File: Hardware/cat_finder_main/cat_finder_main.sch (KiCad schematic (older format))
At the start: 32 parts, among them J1 BATT, J10 Analog, J2 BME280, J3 CSS811, J4 DRIVERS, J5 GY-87, J6 Prog, J7 FTDI, J8 Digital, J9 i2c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

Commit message: clone other repo
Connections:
- net INTCSS is gone; now on net +3V3: J3.6 (Pin_6)
- net RESET is gone; now on net +3V3: J3.7 (Pin_7)
- net WAKE is gone; now on net GND: J3.5 (Pin_5)
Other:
- moved on the sheet: JP10, JP5, JP6, JP7, JP8, JP9
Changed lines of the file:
@@
 	1760 6310 2010 6310
-$Comp
-L power:GND #PWR09
-U 1 1 5D24666B
-P 3280 6200
-F 0 "#PWR09" H 3280 5950 50  0001 C CNN
-F 1 "GND" H 3285 6027 50  0000 C CNN
-F 2 "" H 3280 6200 50  0001 C CNN
-F 3 "" H 3280 6200 50  0001 C CNN
-	1    3280 6200
-	1    0    0    -1
-$EndComp
 $Comp
 L power:+3.3V #PWR08
@@
 Wire Wire Line
 	3280 6060 3570 6060
-Wire Wire Line
-	3280 6200 3280 6160
-Wire Wire Line
-	3280 6160 3570 6160
 $Comp
 L rover_main-rescue:MCP732831CHARGER-electroniccats U2
@@
 	0    -1   -1   0
 $EndComp
-Text Label 10400 4800 0    50   ~ 0
+Text Label 10760 4600 0    50   ~ 0
 SCL
-Text Label 10400 4400 0    50   ~ 0
+Text Label 10760 4300 0    50   ~ 0
 SDA
-Text Label 9800 4400 2    50   ~ 0
+Text Label 10160 4300 2    50   ~ 0
 SDAB
 Text Label 8450 6050 3    50   ~ 0
 SDAB
-Text Label 9800 4800 2    50   ~ 0
+Text Label 10160 4600 2    50   ~ 0
 SCLB
 Text Label 8550 6050 3    50   ~ 0
 SCLB
-Text Label 9800 6000 2    50   ~ 0
+Text Label 10150 5500 2    50   ~ 0
 A3
-Text Label 10400 5600 0    50   ~ 0
+Text Label 10750 5210 0    50   ~ 0
 GPIO12
-Text Label 10400 5200 0    50   ~ 0
+Text Label 10750 4900 0    50   ~ 0
 GPIO13
-Text Label 10400 6000 0    50   ~ 0
+Text Label 10750 5500 0    50   ~ 0
 GPIO15
-Text Label 10380 6400 0    50   ~ 0
+Text Label 10700 5800 0    50   ~ 0
 GPIO14
 $Comp
@@
 Text Label 5290 6000 2    50   ~ 0
 VCC-IN
-Text Label 9800 5600 2    50   ~ 0
+Text Label 10150 5210 2    50   ~ 0
 11
-Text Label 9800 5200 2    50   ~ 0
+Text Label 10150 4900 2    50   ~ 0
 A1
-Text Label 9820 6400 2    50   ~ 0
+Text Label 10140 5800 2    50   ~ 0
 9
 $Comp
@@
 L Device:Jumper_NO_Small JP5
 U 1 1 5D4C5CB0
-P 10080 4400
-F 0 "JP5" H 10080 4585 50  0000 C CNN
-F 1 "SDA" H 10080 4494 50  0000 C CNN
-F 2 "Jumper:SolderJumper-2_P1.3mm_Open_RoundedPad1.0x1.5mm" H 10080 4400 50  0001 C CNN
-F 3 "~" H 10080 4400 50  0001 C CNN
-	1    10080 4400
+P 10440 4300
+F 0 "JP5" H 10440 4485 50  0000 C CNN
+F 1 "SDA" H 10440 4394 50  0000 C CNN
+F 2 "Jumper:SolderJumper-2_P1.3mm_Open_RoundedPad1.0x1.5mm" H 10440 4300 50  0001 C CNN
+F 3 "~" H 10440 4300 50  0001 C CNN
+	1    10440 4300
 	1    0    0    -1
 $EndComp
@@
 L Device:Jumper_NO_Small JP6
 U 1 1 5D4C667E
-P 10100 4800
-F 0 "JP6" H 10100 4985 50  0000 C CNN
-F 1 "SCL" H 10100 4894 50  0000 C CNN
-F 2 "Jumper:SolderJumper-2_P1.3mm_Open_RoundedPad1.0x1.5mm" H 10100 4800 50  0001 C CNN
-F 3 "~" H 10100 4800 50  0001 C CNN
-	1    10100 4800
-	1    0    0    -1
-$EndComp
-Wire Wire Line
-	10180 4400 10400 4400
-Wire Wire Line
-	9980 4400 9800 4400
-Wire Wire Line
-	10400 4800 10200 4800
-Wire Wire Line
-	9800 4800 10000 4800
+P 10460 4600
+F 0 "JP6" H 10460 4785 50  0000 C CNN
+F 1 "SCL" H 10460 4694 50  0000 C CNN
+F 2 "Jumper:SolderJumper-2_P1.3mm_Open_RoundedPad1.0x1.5mm" H 10460 4600 50  0001 C CNN
+F 3 "~" H 10460 4600 50  0001 C CNN
+	1    10460 4600
+	1    0    0    -1
+$EndComp
+Wire Wire Line
+	10540 4300 10760 4300
+Wire Wire Line
+	10340 4300 10160 4300
+Wire Wire Line
+	10760 4600 10560 4600
+Wire Wire Line
+	10160 4600 10360 4600
 $Comp
 L Device:Jumper_NO_Small JP7
 U 1 1 5D4CD611
-P 10120 5200
-F 0 "JP7" H 10120 5385 50  0000 C CNN
-F 1 "Engine 1 A" H 10120 5294 50  0000 C CNN
-F 2 "Jumper:SolderJumper-2_P1.3mm_Open_RoundedPad1.0x1.5mm" H 10120 5200 50  0001 C CNN
-F 3 "~" H 10120 5200 50  0001 C CNN
-	1    10120 5200
-	1    0    0    -1
-$EndComp
-Wire Wire Line
-	10220 5200 10400 5200
-Wire Wire Line
-	10020 5200 9800 5200
+P 10470 4900
+F 0 "JP7" H 10470 5085 50  0000 C CNN
+F 1 "Engine 1 A" H 10470 4994 50  0000 C CNN
+F 2 "Jumper:SolderJumper-2_P1.3mm_Open_RoundedPad1.0x1.5mm" H 10470 4900 50  0001 C CNN
+F 3 "~" H 10470 4900 50  0001 C CNN
+	1    10470 4900
+	1    0    0    -1
+$EndComp
+Wire Wire Line
+	10570 4900 10750 4900
+Wire Wire Line
+	10370 4900 10150 4900
 $Comp
 L Device:Jumper_NO_Small JP8
 U 1 1 5D4D2033
-P 10130 5600
-F 0 "JP8" H 10130 5785 50  0000 C CNN
-F 1 "Engine 1B" H 10130 5694 50  0000 C CNN
-F 2 "Jumper:SolderJumper-2_P1.3mm_Open_RoundedPad1.0x1.5mm" H 10130 5600 50  0001 C CNN
-F 3 "~" H 10130 5600 50  0001 C CNN
-	1    10130 5600
-	1    0    0    -1
-$EndComp
-Wire Wire Line
-	10230 5600 10400 5600
-Wire Wire Line
-	10030 5600 9800 5600
+P 10480 5210
+F 0 "JP8" H 10480 5395 50  0000 C CNN
+F 1 "Engine 1B" H 10480 5304 50  0000 C CNN
+F 2 "Jumper:SolderJumper-2_P1.3mm_Open_RoundedPad1.0x1.5mm" H 10480 5210 50  0001 C CNN
+F 3 "~" H 10480 5210 50  0001 C CNN
+	1    10480 5210
+	1    0    0    -1
+$EndComp
+Wire Wire Line
+	10580 5210 10750 5210
+Wire Wire Line
+	10380 5210 10150 5210
 $Comp
 L Device:Jumper_NO_Small JP9
 U 1 1 5D4D5761
-P 10100 6000
-F 0 "JP9" H 10100 6185 50  0000 C CNN
-F 1 "Engine 2A" H 10100 6094 50  0000 C CNN
-F 2 "Jumper:SolderJumper-2_P1.3mm_Open_RoundedPad1.0x1.5mm" H 10100 6000 50  0001 C CNN
-F 3 "~" H 10100 6000 50  0001 C CNN
-	1    10100 6000
-	1    0    0    -1
-$EndComp
-Wire Wire Line
-	10200 6000 10400 6000
-Wire Wire Line
-	9800 6000 10000 6000
+P 10450 5500
+F 0 "JP9" H 10450 5685 50  0000 C CNN
+F 1 "Engine 2A" H 10450 5594 50  0000 C CNN
+F 2 "Jumper:SolderJumper-2_P1.3mm_Open_RoundedPad1.0x1.5mm" H 10450 5500 50  0001 C CNN
+F 3 "~" H 10450 5500 50  0001 C CNN
+	1    10450 5500
+	1    0    0    -1
+$EndComp
+Wire Wire Line
+	10550 5500 10750 5500
+Wire Wire Line
+	10150 5500 10350 5500
 $Comp
 L Device:Jumper_NO_Small JP10
 U 1 1 5D4DA54D
-P 10100 6400
-F 0 "JP10" H 10100 6585 50  0000 C CNN
-F 1 "Engine 2B" H 10100 6494 50  0000 C CNN
-F 2 "Jumper:SolderJumper-2_P1.3mm_Open_RoundedPad1.0x1.5mm" H 10100 6400 50  0001 C CNN
-F 3 "~" H 10100 6400 50  0001 C CNN
-	1    10100 6400
-	1    0    0    -1
-$EndComp
-Wire Wire Line
-	10200 6400 10380 6400
-Wire Wire Line
-	10000 6400 9820 6400
+P 10420 5800
+F 0 "JP10" H 10420 5985 50  0000 C CNN
+F 1 "Engine 2B" H 10420 5894 50  0000 C CNN
+F 2 "Jumper:SolderJumper-2_P1.3mm_Open_RoundedPad1.0x1.5mm" H 10420 5800 50  0001 C CNN
+F 3 "~" H 10420 5800 50  0001 C CNN
+	1    10420 5800
+	1    0    0    -1
+$EndComp
+Wire Wire Line
+	10520 5800 10700 5800
+Wire Wire Line
+	10320 5800 10140 5800
+$Comp
+L power:+3.3V #PWR?
+U 1 1 5D54B969
+P 3000 6400
+F 0 "#PWR?" H 3000 6250 50  0001 C CNN
+F 1 "+3.3V" H 2840 6420 50  0000 C CNN
+F 2 "" H 3000 6400 50  0001 C CNN
+F 3 "" H 3000 6400 50  0001 C CNN
+	1    3000 6400
+	1    0    0    -1
+$EndComp
+$Comp
+L power:GND #PWR?
+U 1 1 5D544C06
+P 3200 6470
+F 0 "#PWR?" H 3200 6220 50  0001 C CNN
+F 1 "GND" H 3100 6470 50  0000 C CNN
+F 2 "" H 3200 6470 50  0001 C CNN
+F 3 "" H 3200 6470 50  0001 C CNN
+	1    3200 6470
+	1    0    0    -1
+$EndComp
+Wire Wire Line
+	3570 6460 3200 6460
+Wire Wire Line
+	3200 6460 3200 6470
+Wire Wire Line
+	3570 6160 3200 6160
+Wire Wire Line
+	3200 6160 3200 6460
+Connection ~ 3200 6460
+Wire Wire Line
+	3570 6560 3300 6560
+Wire Wire Line
+	3300 6560 3300 6660
+Wire Wire Line
+	3300 6660 3570 6660
+Wire Wire Line
+	3300 6660 3000 6660
+Connection ~ 3300 6660
+Wire Wire Line
+	3000 6660 3000 6400
 $EndSCHEMATC

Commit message: fix charger
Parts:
- removed U2: MCP732831CHARGER, Batteries:charger_EC_3.3V_battery, symbol rover_main-rescue:MCP732831CHARGER-electroniccats
- added U2: MCP732831CHARGER, Batteries:charger_EC_3.3V_battery, symbol electroniccats:MCP732831CHARGER
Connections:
- net BATT: now also U2.3 (OUT)
- net GND: now also U2.2 (GND), U2.4 (GND)
- net VCC: now also U2.1 (VCC)
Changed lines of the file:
@@
 EESchema Schematic File Version 4
-LIBS:rover_main-cache
 EELAYER 29 0
 EELAYER END
@@
 	3280 6060 3570 6060
 $Comp
-L rover_main-rescue:MCP732831CHARGER-electroniccats U2
-U 1 1 5D24ED12
-P 4180 3790
-F 0 "U2" H 4180 4205 50  0000 C CNN
-F 1 "MCP732831CHARGER" H 4180 4114 50  0000 C CNN
-F 2 "Batteries:charger_EC_3.3V_battery" H 4180 3790 50  0001 C CNN
-F 3 "" H 4180 3790 50  0001 C CNN
-F 4 "EC" H 4180 3790 50  0001 C CNN "manf#"
-	1    4180 3790
-	1    0    0    -1
-$EndComp
-$Comp
 L power:VCC #PWR05
 U 1 1 5D24F7E2
@@
 Wire Wire Line
 	3000 6660 3000 6400
+$Comp
+L electroniccats:MCP732831CHARGER U2
+U 1 1 5D6C735F
+P 4180 3790
+F 0 "U2" H 4180 4205 50  0000 C CNN
+F 1 "MCP732831CHARGER" H 4180 4114 50  0000 C CNN
+F 2 "Batteries:charger_EC_3.3V_battery" H 4180 3790 50  0001 C CNN
+F 3 "" H 4180 3790 50  0001 C CNN
+F 4 "EC" H 4180 3790 50  0001 C CNN "manf#"
+	1    4180 3790
+	1    0    0    -1
+$EndComp
 $EndSCHEMATC

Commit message: change drill esp32
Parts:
- removed U3: ESP32-CAM, Rf:ESP32-CAM, symbol rover_main-rescue:ESP32-CAM-electroniccats
- added U3: ESP32-CAM, Rf:ESP32-CAM, symbol electroniccats:ESP32-CAM
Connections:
- net +3V3: now also U3.8 (3V3)
- net 3.3V-5V: now also U3.4 (VCC)
- net 5V: now also U3.9 (5V)
- net GND: now also U3.1 (GND), U3.10 (GND), U3.5 (GND)
- net GPIO0: now also U3.6 (IO0)
- net GPIO12E: now also U3.11 (IO12)
- net GPIO13E: now also U3.12 (IO13)
- net GPIO14E: now also U3.14 (IO14)
- net GPIO15E: now also U3.13 (IO15)
- net GPIO2: now also U3.15 (IO2)
- net GPIO4: now also U3.16 (IO4)
- net RX: now also U3.3 (UnR)
- net SCLE: now also U3.7 (IO16)
- net TX: now also U3.2 (UoT)
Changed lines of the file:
@@
-	1    0    0    -1
-$EndComp
-$Comp
-L rover_main-rescue:ESP32-CAM-electroniccats U3
-U 1 1 5D363E9F
-P 9080 1350
-F 0 "U3" H 9080 1865 50  0000 C CNN
-F 1 "ESP32-CAM" H 9080 1774 50  0000 C CNN
-F 2 "Rf:ESP32-CAM" H 9080 1350 50  0001 C CNN
-F 3 "" H 9080 1350 50  0001 C CNN
-	1    9080 1350
 	1    0    0    -1
 $EndComp
@@
 	10320 5800 10140 5800
 $Comp
-L power:+3.3V #PWR?
+L power:+3.3V #PWR0101
 U 1 1 5D54B969
 P 3000 6400
-F 0 "#PWR?" H 3000 6250 50  0001 C CNN
+F 0 "#PWR0101" H 3000 6250 50  0001 C CNN
 F 1 "+3.3V" H 2840 6420 50  0000 C CNN
 F 2 "" H 3000 6400 50  0001 C CNN
@@
 $EndComp
 $Comp
-L power:GND #PWR?
+L power:GND #PWR0102
 U 1 1 5D544C06
 P 3200 6470
-F 0 "#PWR?" H 3200 6220 50  0001 C CNN
+F 0 "#PWR0102" H 3200 6220 50  0001 C CNN
 F 1 "GND" H 3100 6470 50  0000 C CNN
 F 2 "" H 3200 6470 50  0001 C CNN
@@
 	1    0    0    -1
 $EndComp
+$Comp
+L electroniccats:ESP32-CAM U3
+U 1 1 5D6F0550
+P 9080 1350
+F 0 "U3" H 9080 1865 50  0000 C CNN
+F 1 "ESP32-CAM" H 9080 1774 50  0000 C CNN
+F 2 "Rf:ESP32-CAM" H 9080 1350 50  0001 C CNN
+F 3 "" H 9080 1350 50  0001 C CNN
+	1    9080 1350
+	1    0    0    -1
+$EndComp

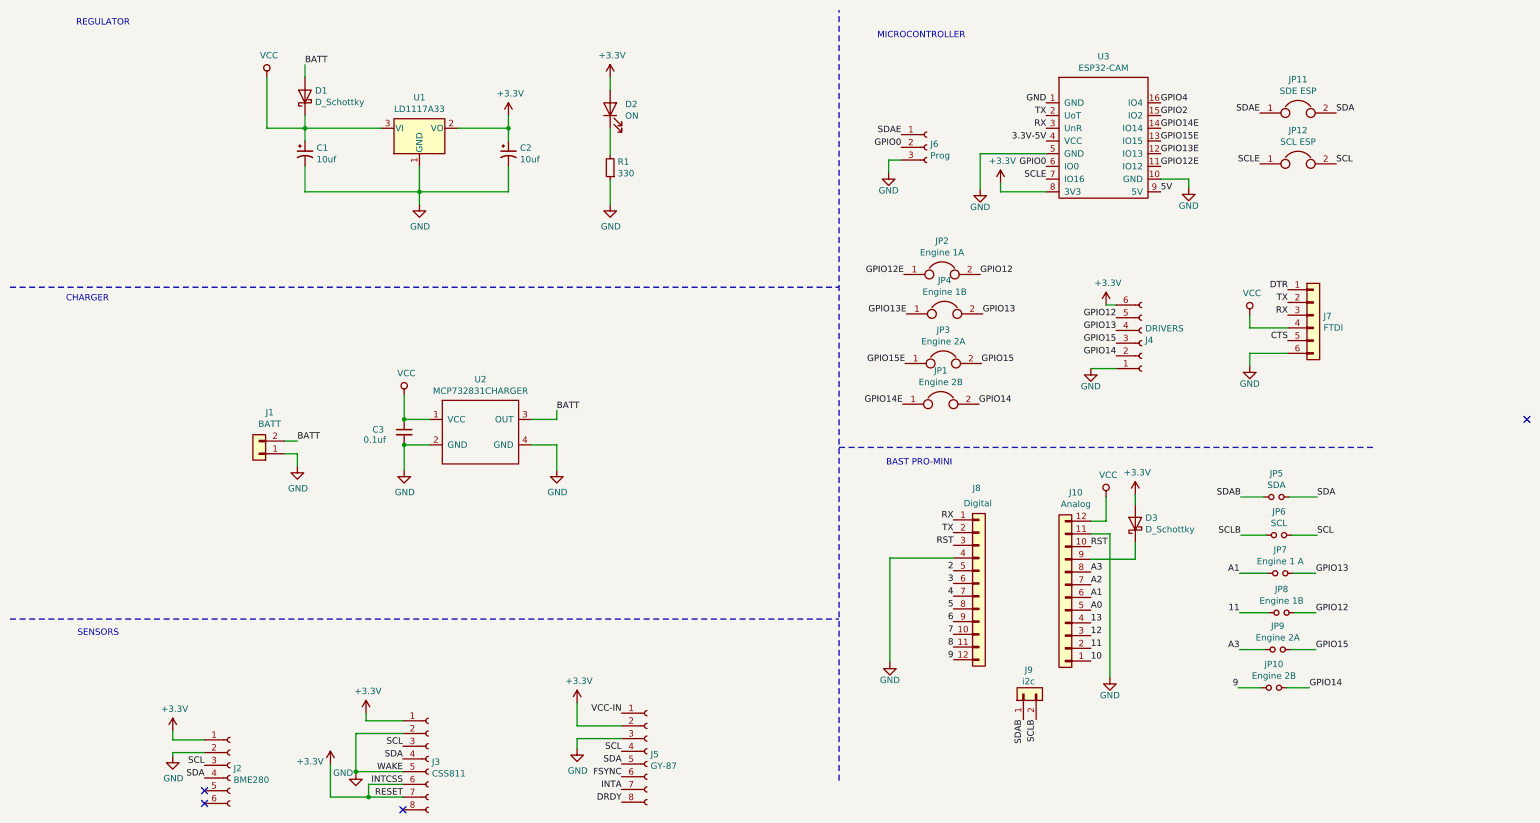
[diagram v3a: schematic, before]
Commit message: add switch
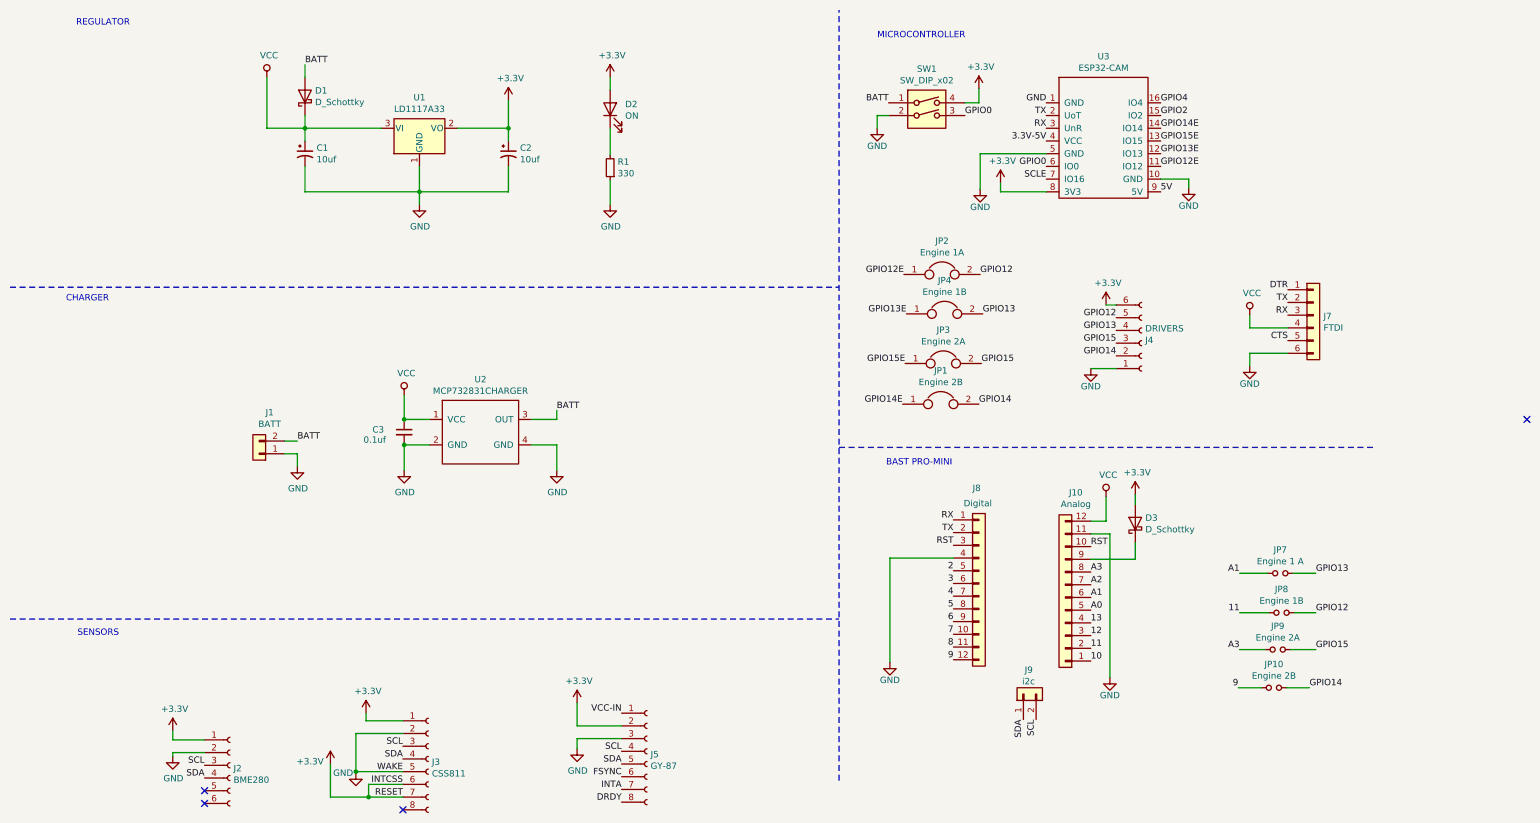
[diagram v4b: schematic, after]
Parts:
- removed J6: Prog, Connector_PinHeader_2.54mm:PinHeader_1x03_P2.54mm_Vertical, symbol Connector:Conn_01x03_Female
- removed JP11: SDE ESP, Jumper:SolderJumper-2_P1.3mm_Bridged_RoundedPad1.0x1.5mm, symbol Device:Jumper
- removed JP12: SCL ESP, Jumper:SolderJumper-2_P1.3mm_Bridged_RoundedPad1.0x1.5mm, symbol Device:Jumper
- removed JP5: SDA, Jumper:SolderJumper-2_P1.3mm_Open_RoundedPad1.0x1.5mm, symbol Device:Jumper_NO_Small
- removed JP6: SCL, Jumper:SolderJumper-2_P1.3mm_Open_RoundedPad1.0x1.5mm, symbol Device:Jumper_NO_Small
- added SW1: SW_DIP_x02, connectors:DP-02, symbol Switch:SW_DIP_x02
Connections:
- net SCLB is gone; now on net SCL: J9.2 (Pin_2)
- net SDAB is gone; now on net SDA: J9.1 (Pin_1)
- net +3V3: now also SW1.4
- net BATT: now also SW1.1
- net GND: now also SW1.2
- net GPIO0: now also SW1.3
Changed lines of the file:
@@
 Wire Wire Line
 	2800 900  2800 1000
-$Comp
-L power:+3.3V #PWR010
-U 1 1 5D24B77A
-P 4400 1300
-F 0 "#PWR010" H 4400 1150 50  0001 C CNN
-F 1 "+3.3V" H 4415 1473 50  0000 C CNN
-F 2 "" H 4400 1300 50  0001 C CNN
-F 3 "" H 4400 1300 50  0001 C CNN
-	1    4400 1300
-	1    0    0    -1
-$EndComp
 Wire Wire Line
 	4400 1700 4400 1900
@@
 Wire Wire Line
 	4400 1400 4400 1500
-Wire Wire Line
-	4400 1300 4400 1400
 Connection ~ 4400 1400
 $Comp
@@
 Wire Wire Line
 	8980 3290 9180 3290
-Text Label 10910 1280 0    50   ~ 0
-SDA
 Text Label 8630 1800 2    50   ~ 0
 SCLE
@@
 L power:GND #PWR023
 U 1 1 5D494473
-P 7390 1750
-F 0 "#PWR023" H 7390 1500 50  0001 C CNN
-F 1 "GND" H 7390 1610 50  0000 C CNN
-F 2 "" H 7390 1750 50  0001 C CNN
-F 3 "" H 7390 1750 50  0001 C CNN
-	1    7390 1750
-	1    0    0    -1
-$EndComp
-Text Label 7490 1550 2    50   ~ 0
+P 7300 1400
+F 0 "#PWR023" H 7300 1150 50  0001 C CNN
+F 1 "GND" H 7300 1260 50  0000 C CNN
+F 2 "" H 7300 1400 50  0001 C CNN
+F 3 "" H 7300 1400 50  0001 C CNN
+	1    7300 1400
+	1    0    0    -1
+$EndComp
+Text Label 7990 1300 0    50   ~ 0
 GPIO0
-Wire Wire Line
-	7390 1750 7390 1650
-Wire Wire Line
-	7390 1650 7490 1650
-$Comp
-L Device:Jumper JP11
-U 1 1 5D49CFDF
-P 10610 1280
-F 0 "JP11" H 10610 1544 50  0000 C CNN
-F 1 "SDE ESP" H 10610 1453 50  0000 C CNN
-F 2 "Jumper:SolderJumper-2_P1.3mm_Bridged_RoundedPad1.0x1.5mm" H 10610 1280 50  0001 C CNN
-F 3 "~" H 10610 1280 50  0001 C CNN
-	1    10610 1280
-	1    0    0    -1
-$EndComp
-Text Label 10310 1280 2    50   ~ 0
-SDAE
-Text Label 7490 1450 2    50   ~ 0
-SDAE
-$Comp
-L Device:Jumper JP12
-U 1 1 5D4A0E2A
-P 10610 1680
-F 0 "JP12" H 10610 1944 50  0000 C CNN
-F 1 "SCL ESP" H 10610 1853 50  0000 C CNN
-F 2 "Jumper:SolderJumper-2_P1.3mm_Bridged_RoundedPad1.0x1.5mm" H 10610 1680 50  0001 C CNN
-F 3 "~" H 10610 1680 50  0001 C CNN
-	1    10610 1680
-	1    0    0    -1
-$EndComp
-Text Label 10910 1680 0    50   ~ 0
-SCL
-Text Label 10310 1680 2    50   ~ 0
-SCLE
 Wire Notes Line
 	7000 3910 11220 3910
@@
 	0    -1   -1   0
 $EndComp
-Text Label 10760 4600 0    50   ~ 0
+Text Label 8450 6050 3    50   ~ 0
+SDA
+Text Label 8550 6050 3    50   ~ 0
 SCL
-Text Label 10760 4300 0    50   ~ 0
-SDA
-Text Label 10160 4300 2    50   ~ 0
-SDAB
-Text Label 8450 6050 3    50   ~ 0
-SDAB
-Text Label 10160 4600 2    50   ~ 0
-SCLB
-Text Label 8550 6050 3    50   ~ 0
-SCLB
 Text Label 10150 5500 2    50   ~ 0
 A3
@@
 Wire Wire Line
 	9330 4660 9330 4790
-$Comp
-L Connector:Conn_01x03_Female J6
-U 1 1 5D4B08DF
-P 7690 1550
-F 0 "J6" H 7718 1576 50  0000 L CNN
-F 1 "Prog" H 7718 1485 50  0000 L CNN
-F 2 "Connector_PinHeader_2.54mm:PinHeader_1x03_P2.54mm_Vertical" H 7690 1550 50  0001 C CNN
-F 3 "~" H 7690 1550 50  0001 C CNN
-	1    7690 1550
-	1    0    0    -1
-$EndComp
 Text Label 9530 1300 0    50   ~ 0
 GPIO2
 Text Notes 7370 4060 0    50   ~ 0
 BAST PRO-MINI\n
-$Comp
-L Device:Jumper_NO_Small JP5
-U 1 1 5D4C5CB0
-P 10440 4300
-F 0 "JP5" H 10440 4485 50  0000 C CNN
-F 1 "SDA" H 10440 4394 50  0000 C CNN
-F 2 "Jumper:SolderJumper-2_P1.3mm_Open_RoundedPad1.0x1.5mm" H 10440 4300 50  0001 C CNN
-F 3 "~" H 10440 4300 50  0001 C CNN
-	1    10440 4300
-	1    0    0    -1
-$EndComp
-$Comp
-L Device:Jumper_NO_Small JP6
-U 1 1 5D4C667E
-P 10460 4600
-F 0 "JP6" H 10460 4785 50  0000 C CNN
-F 1 "SCL" H 10460 4694 50  0000 C CNN
-F 2 "Jumper:SolderJumper-2_P1.3mm_Open_RoundedPad1.0x1.5mm" H 10460 4600 50  0001 C CNN
-F 3 "~" H 10460 4600 50  0001 C CNN
-	1    10460 4600
-	1    0    0    -1
-$EndComp
-Wire Wire Line
-	10540 4300 10760 4300
-Wire Wire Line
-	10340 4300 10160 4300
-Wire Wire Line
-	10760 4600 10560 4600
-Wire Wire Line
-	10160 4600 10360 4600
 $Comp
 L Device:Jumper_NO_Small JP7
@@
 	1    0    0    -1
 $EndComp
+$Comp
+L Switch:SW_DIP_x02 SW1
+U 1 1 5D6FB55A
+P 7690 1300
+F 0 "SW1" H 7690 1667 50  0000 C CNN
+F 1 "SW_DIP_x02" H 7690 1576 50  0000 C CNN
+F 2 "connectors:DP-02" H 7690 1300 50  0001 C CNN
+F 3 "~" H 7690 1300 50  0001 C CNN
+	1    7690 1300
+	1    0    0    -1
+$EndComp
+Wire Wire Line
+	7300 1400 7300 1300
+Wire Wire Line
+	7300 1300 7390 1300
+Text Label 7390 1200 2    50   ~ 0
+BATT
+$Comp
+L power:+3.3V #PWR?
+U 1 1 5D736D41
+P 8100 1090
+F 0 "#PWR?" H 8100 940 50  0001 C CNN
+F 1 "+3.3V" H 8115 1263 50  0000 C CNN
+F 2 "" H 8100 1090 50  0001 C CNN
+F 3 "" H 8100 1090 50  0001 C CNN
+	1    8100 1090
+	1    0    0    -1
+$EndComp
+Wire Wire Line
+	7990 1200 8100 1200
+Wire Wire Line
+	8100 1200 8100 1090
+$Comp
+L power:+3.3V #PWR?
+U 1 1 5D739360
+P 4400 1180
+F 0 "#PWR?" H 4400 1030 50  0001 C CNN
+F 1 "+3.3V" H 4415 1353 50  0000 C CNN
+F 2 "" H 4400 1180 50  0001 C CNN
+F 3 "" H 4400 1180 50  0001 C CNN
+	1    4400 1180
+	1    0    0    -1
+$EndComp
+Wire Wire Line
+	4400 1180 4400 1400
 $EndSCHEMATC
